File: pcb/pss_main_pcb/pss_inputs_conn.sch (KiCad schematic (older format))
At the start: 8 parts

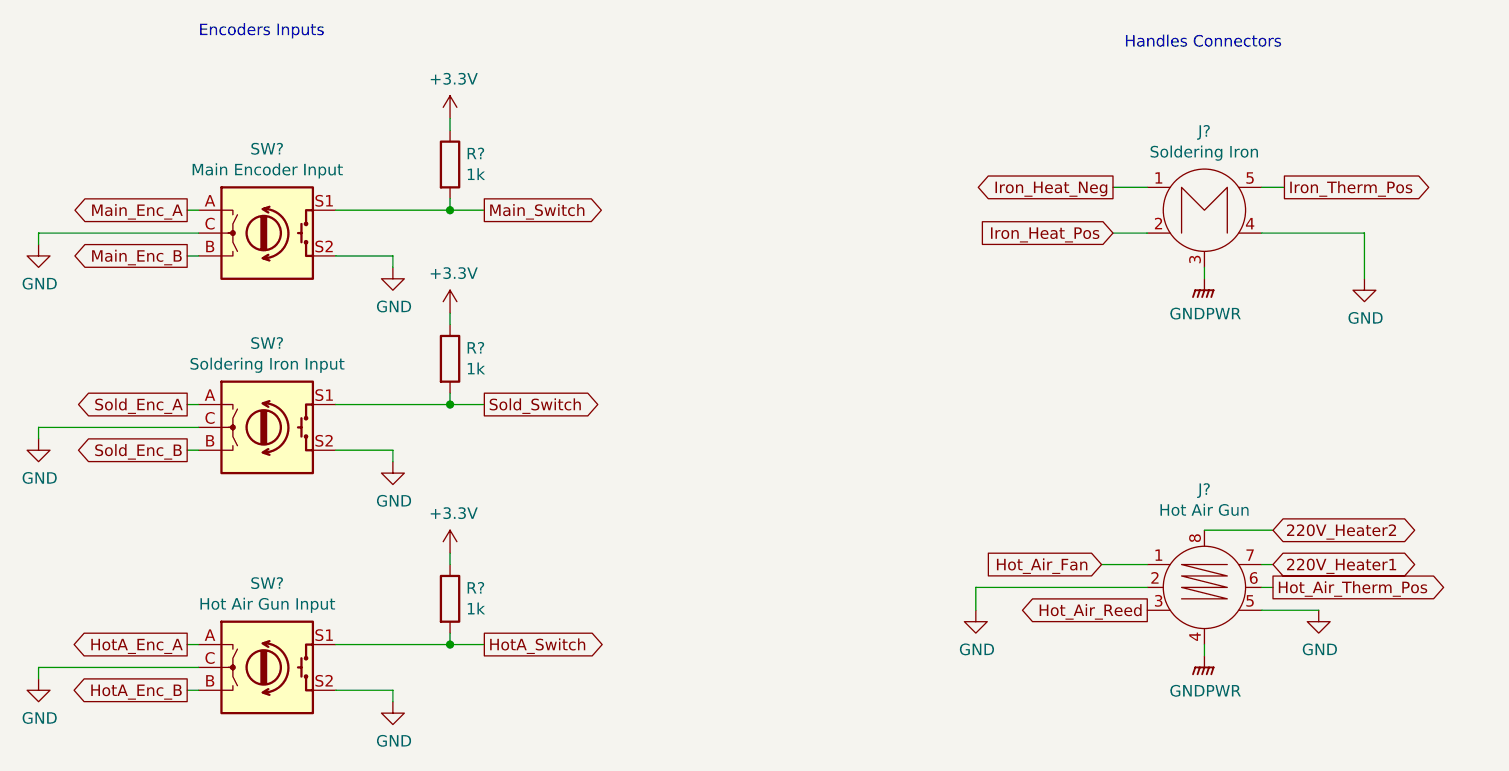
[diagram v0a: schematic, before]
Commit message: Add stm32 schematics
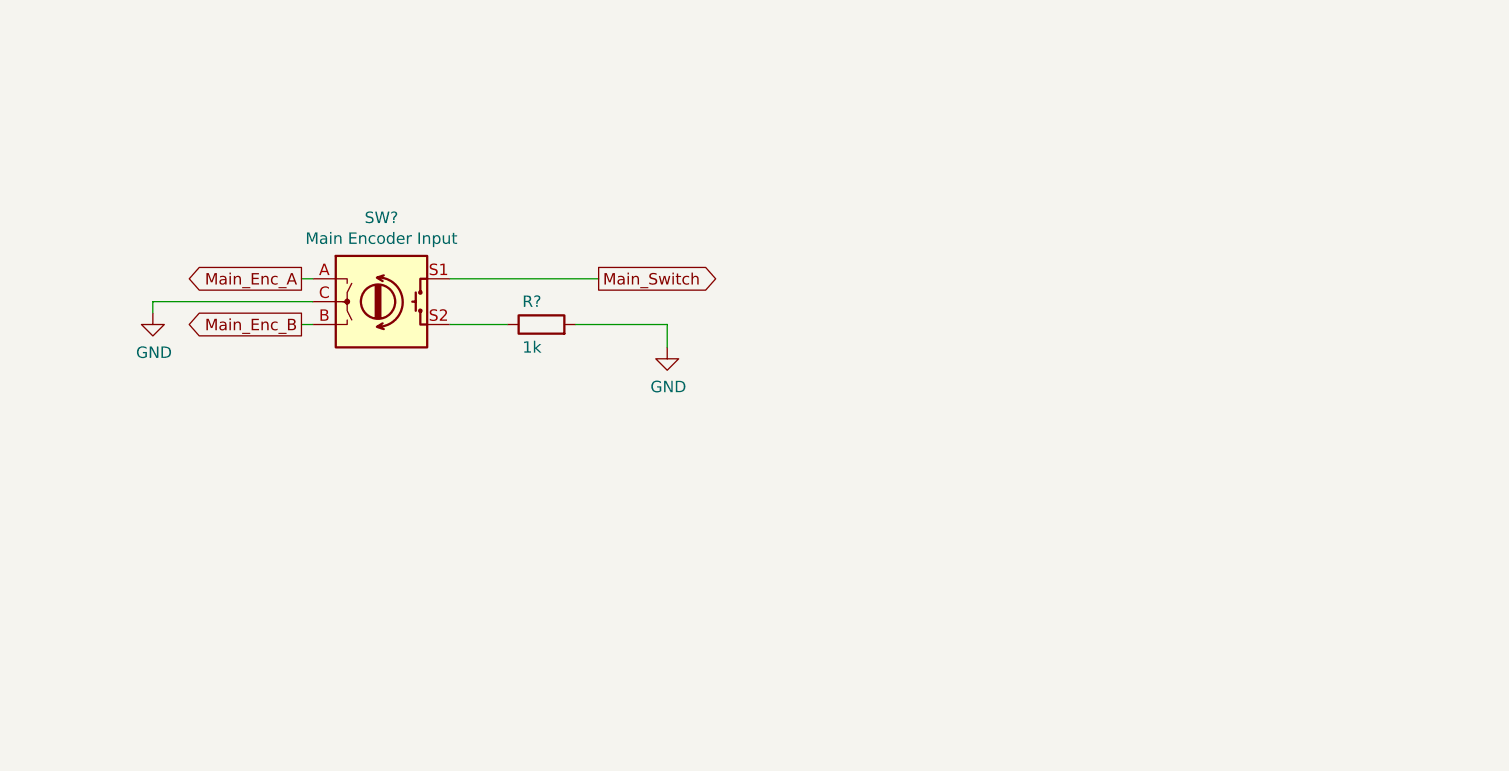
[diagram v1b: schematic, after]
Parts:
- removed J?: Soldering Iron, symbol gx16_conn:GX16-M5_connector
- removed J?: Hot Air Gun, symbol gx16_conn:GX16-M8_connector
- removed R? (x3): 1k, symbol Device:R
- removed SW?: Main Encoder Input, symbol Device:Rotary_Encoder_Switch
- removed SW?: Soldering Iron Input, symbol Device:Rotary_Encoder_Switch
- removed SW?: Hot Air Gun Input, symbol Device:Rotary_Encoder_Switch
- added R?: 1k, symbol Device:R
- added SW?: Main Encoder Input, symbol Device:Rotary_Encoder_Switch
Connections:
- net GND: now also R?.2, SW?.C
- net Main_Enc_A: now also SW?.A
- net Main_Enc_B: now also SW?.B
- net Main_Switch: now also SW?.S1
- new net: R?.1, SW?.S2
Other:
- note removed: "Encoders Inputs"
- note removed: "Handles Connectors\n"
